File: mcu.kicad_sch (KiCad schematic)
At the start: 44 parts, among them J201 DISP, J202 SWD, J203 SPI, J204 USB serial, Q201 2N7002, SW201 Reset, U201 STM32F103CBT6, U202 USBLC6-2SC6, U203 AMS1117-3.3, Y201 8MHz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

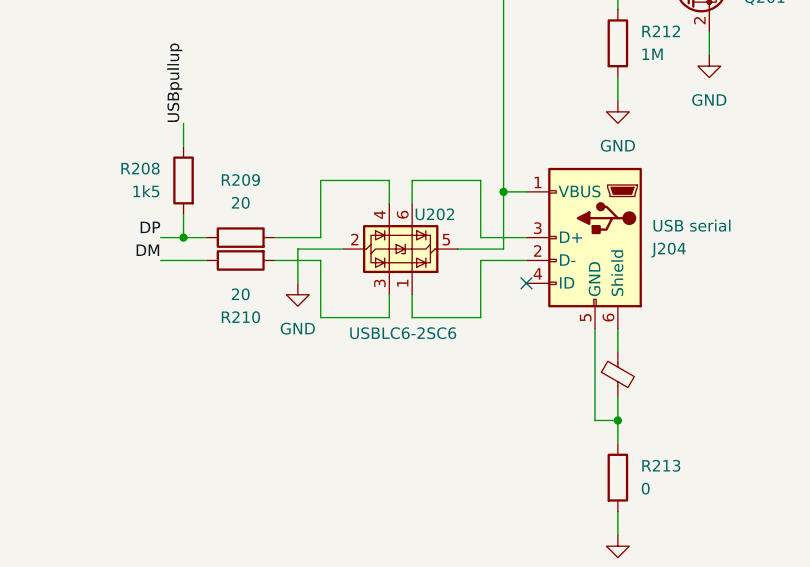
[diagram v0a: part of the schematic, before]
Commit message: Fix USB
Signed-off-by: Benedikt Spranger <b.spranger@linutronix.de>
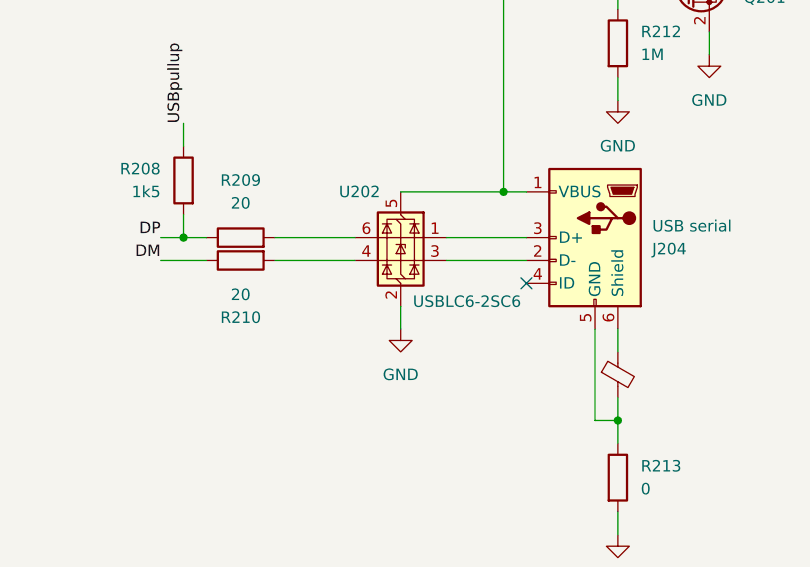
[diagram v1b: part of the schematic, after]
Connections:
- net at U202.1 (I/O1): now also J204.3 (D+); no longer J204.2 (D-)
- net at U202.3 (I/O2): now also J204.2 (D-); no longer R210.2
- net at U202.4 (I/O2): now also R210.2; no longer R209.2
- net at U202.6 (I/O1): now also R209.2; no longer J204.3 (D+)
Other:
- moved on the sheet: U202

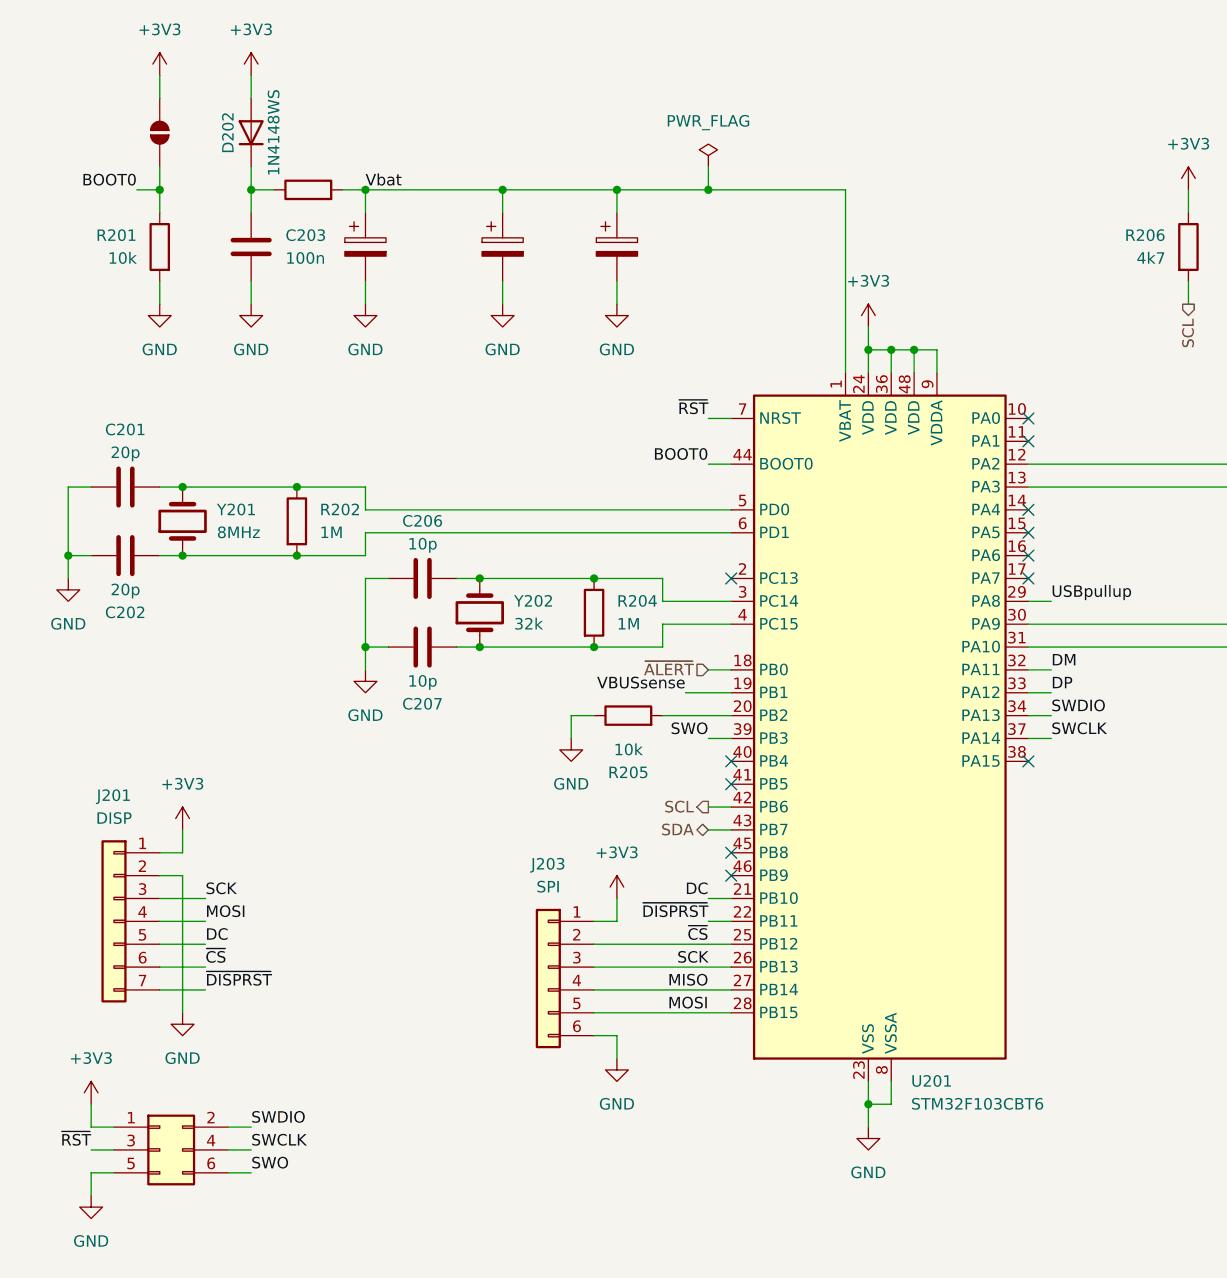
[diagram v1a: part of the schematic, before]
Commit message: Update to KiCAD 9.x
Signed-off-by: Benedikt Spranger <b.spranger@linutronix.de>
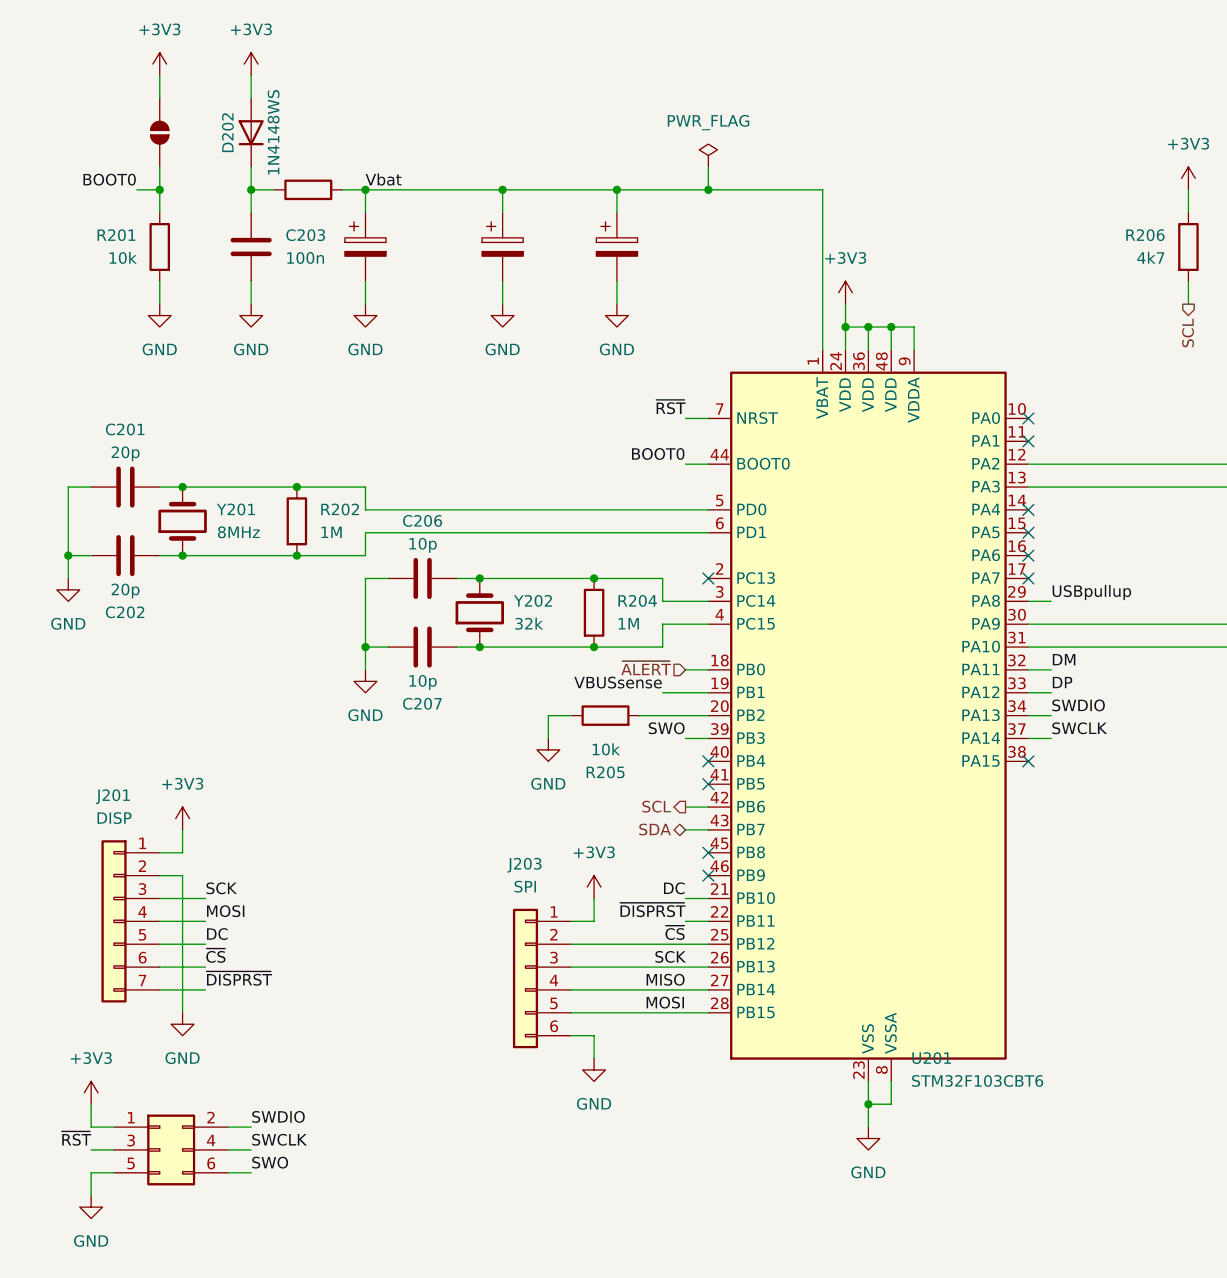
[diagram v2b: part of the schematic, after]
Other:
- moved on the sheet: J203, R205, U201

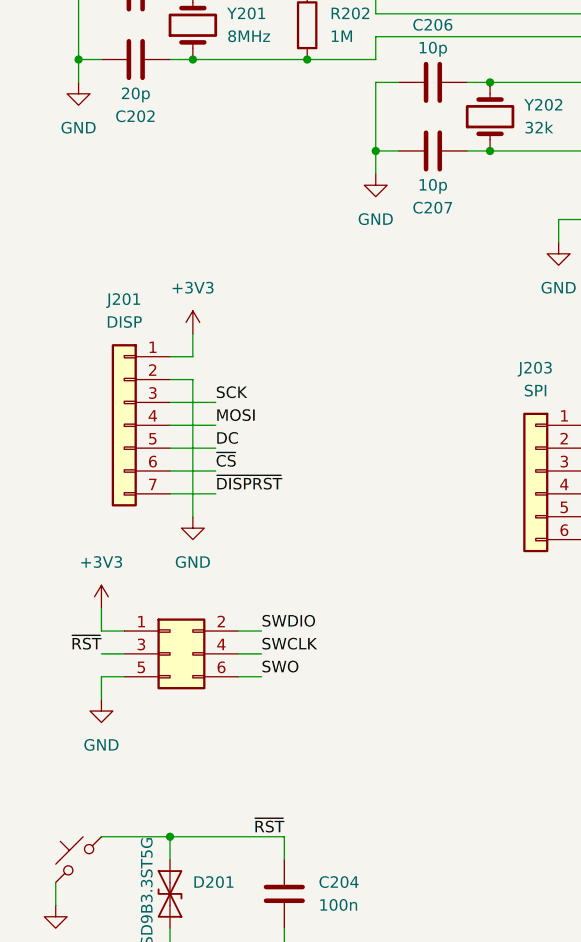
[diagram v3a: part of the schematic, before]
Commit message: Rework SWD connector
Signed-off-by: Benedikt Spranger <b.spranger@linutronix.de>
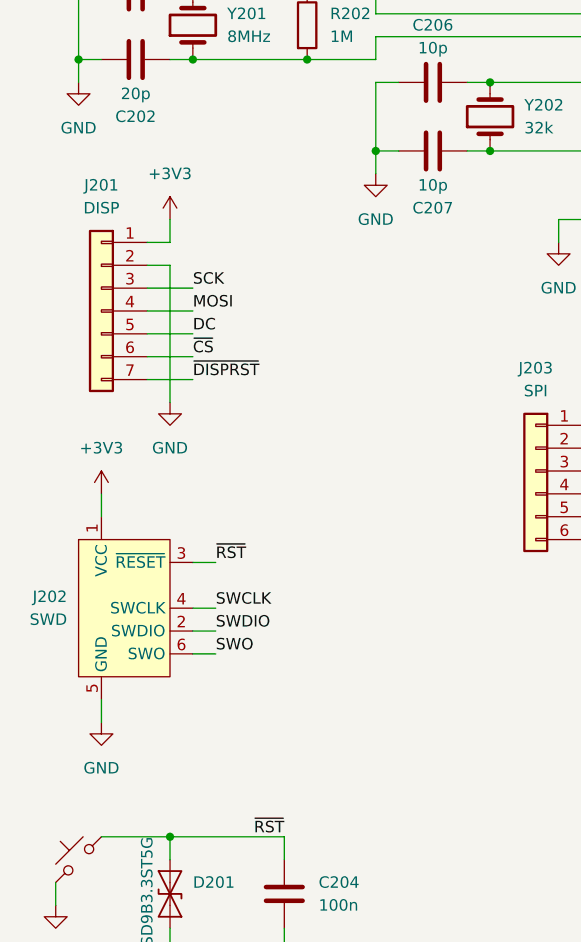
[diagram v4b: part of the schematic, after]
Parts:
- removed J202: SWD, Connector:Tag-Connect_TC2030-IDC-FP_2x03_P1.27mm_Vertical, symbol Connector_Generic:Conn_02x03_Odd_Even
- added J202: SWD, Connector:Tag-Connect_TC2030-IDC-FP_2x03_P1.27mm_Vertical, symbol Connector:Conn_ARM_SWD_TagConnect_TC2030
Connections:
- net +3V3: now also J202.1 (VCC)
- net GND: now also J202.5 (GND)
- net SWCLK: now also J202.4 (SWCLK)
- net SWDIO: now also J202.2 (SWDIO)
- net SWO: now also J202.6 (SWO)
- net ~{RST}: now also J202.3 (~{RESET})
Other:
- moved on the sheet: J201

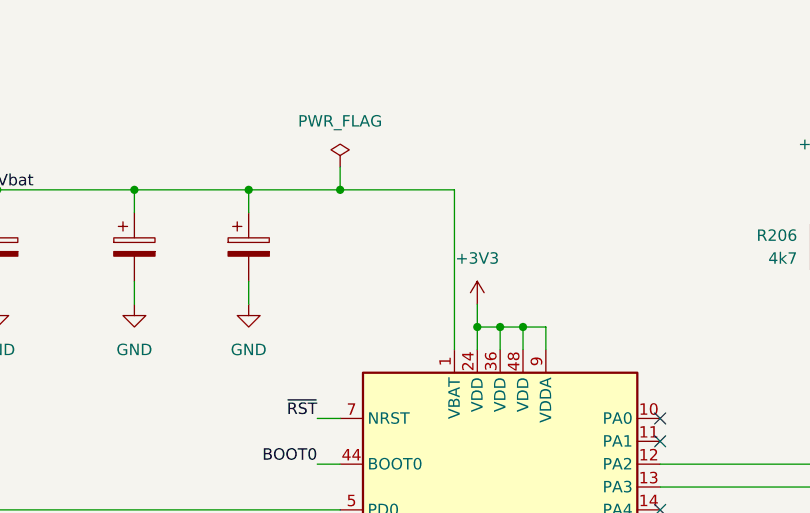
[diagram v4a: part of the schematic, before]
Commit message: Add BAT power disconnector
Signed-off-by: Benedikt Spranger <b.spranger@linutronix.de>
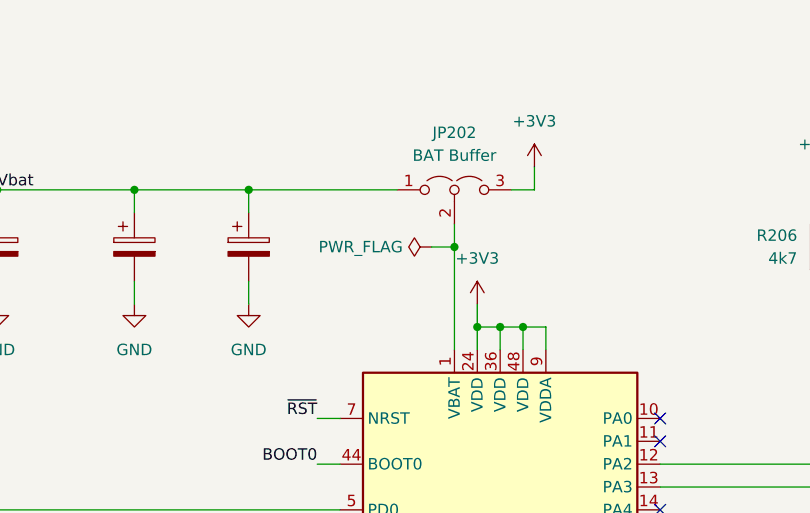
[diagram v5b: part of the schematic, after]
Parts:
- added JP202: BAT Buffer, Connector_PinHeader_2.54mm:PinHeader_1x03_P2.54mm_Vertical, symbol Jumper:Jumper_3_Open
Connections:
- net +3V3: now also JP202.3 (B)
- net Vbat: now also JP202.1 (A); no longer U201.1 (VBAT)
- new net: JP202.2 (C), U201.1 (VBAT)
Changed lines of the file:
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@@
 	)
 	(junction
-		(at 99.06 38.1)
-		(diameter 0)
-		(color 0 0 0 0)
-	)
-	(junction
 		(at 40.64 71.12)
 		(diameter 0)
@@
 	)
 	(junction
+		(at 111.76 44.45)
+		(diameter 0)
+		(color 0 0 0 0)
+	)
+	(junction
 		(at 116.84 139.7)
 		(diameter 0)
@@
 	(wire
 		(pts
+			(xy 111.76 41.91) (xy 111.76 44.45)
+		)
+		(stroke
+			(width 0)
+			(type default)
+		)
+	)
+	(wire
+		(pts
 			(xy 134.62 93.98) (xy 137.16 93.98)
 		)
@@
 	(wire
 		(pts
-			(xy 190.5 38.1) (xy 190.5 40.64)
+			(xy 111.76 44.45) (xy 111.76 55.88)
 		)
 		(stroke
@@
 	(wire
 		(pts
-			(xy 111.76 38.1) (xy 99.06 38.1)
+			(xy 190.5 38.1) (xy 190.5 40.64)
 		)
 		(stroke
@@
 	(wire
 		(pts
+			(xy 118.11 38.1) (xy 120.65 38.1)
+		)
+		(stroke
+			(width 0)
+			(type default)
+		)
+	)
+	(wire
+		(pts
 			(xy 152.4 38.1) (xy 152.4 40.64)
 		)
@@
 	(wire
 		(pts
+			(xy 109.22 44.45) (xy 111.76 44.45)
+		)
+		(stroke
+			(width 0)
+			(type default)
+		)
+	)
+	(wire
+		(pts
 			(xy 76.2 48.26) (xy 76.2 50.8)
 		)
@@
 	(wire
 		(pts
+			(xy 120.65 38.1) (xy 120.65 35.56)
+		)
+		(stroke
+			(width 0)
+			(type default)
+		)
+	)
+	(wire
+		(pts
 			(xy 96.52 68.58) (xy 99.06 68.58)
 		)
@@
 	(wire
 		(pts
-			(xy 88.9 38.1) (xy 99.06 38.1)
+			(xy 88.9 38.1) (xy 105.41 38.1)
 		)
 		(stroke
@@
 	(wire
 		(pts
-			(xy 99.06 35.56) (xy 99.06 38.1)
-		)
-		(stroke
-			(width 0)
-			(type default)
-		)
-	)
-	(wire
-		(pts
 			(xy 83.82 132.08) (xy 86.36 132.08)
 		)
@@
 	(wire
 		(pts
-			(xy 111.76 38.1) (xy 111.76 55.88)
-		)
-		(stroke
-			(width 0)
-			(type default)
-		)
-	)
-	(wire
-		(pts
 			(xy 119.38 53.34) (xy 119.38 55.88)
 		)
@@
 	)
 	(symbol
+		(lib_id "power:+3V3")
+		(at 120.65 35.56 0)
+		(unit 1)
+		(exclude_from_sim no)
+		(in_bom yes)
+		(on_board yes)
+		(dnp no)
+		(fields_autoplaced yes)
+		(property "Reference" "#PWR0242"
+			(at 120.65 39.37 0)
+			(effects
+				(font
+					(size 1.27 1.27)
+				)
+				(hide yes)
+			)
+		)
+		(property "Value" "+3V3"
+			(at 120.65 30.48 0)
+			(effects
+				(font
+					(size 1.27 1.27)
+				)
+			)
+		)
+		(property "Footprint" ""
+			(at 120.65 35.56 0)
+			(effects
+				(font
+					(size 1.27 1.27)
+				)
+				(hide yes)
+			)
+		)
+		(property "Datasheet" ""
+			(at 120.65 35.56 0)
+			(effects
+				(font
+					(size 1.27 1.27)
+				)
+				(hide yes)
+			)
+		)
+		(property "Description" "Power symbol creates a global label with name \"+3V3\""
+			(at 120.65 35.56 0)
+			(effects
+				(font
+					(size 1.27 1.27)
+				)
+				(hide yes)
+			)
+		)
+		(pin "1"
+		)
+		(instances
+			(project "akkupack-ng"
+				(path "/28c14643-513c-46b6-b18d-27cb3c7eee92/de76c23a-5b99-4def-922c-07fd05553b7c"
+					(reference "#PWR0242")
+					(unit 1)
+				)
+			)
+		)
+	)
+	(symbol
 		(lib_id "Device:FerriteBead_Small")
 		(at 254 134.62 0)
@@
 	(symbol
 		(lib_id "power:PWR_FLAG")
-		(at 99.06 35.56 0)
+		(at 109.22 44.45 90)
 		(unit 1)
 		(exclude_from_sim no)
@@
 		(on_board yes)
 		(dnp no)
-		(fields_autoplaced yes)
 		(property "Reference" "#FLG0201"
-			(at 99.06 33.655 0)
+			(at 107.315 44.45 0)
 			(effects
 				(font
@@
 		)
 		(property "Value" "PWR_FLAG"
-			(at 99.06 30.48 0)
+			(at 101.346 44.45 90)
 			(effects
 				(font
@@
 		)
 		(property "Footprint" ""
-			(at 99.06 35.56 0)
+			(at 109.22 44.45 0)
 			(effects
 				(font
@@
 		)
 		(property "Datasheet" "~"
-			(at 99.06 35.56 0)
+			(at 109.22 44.45 0)
 			(effects
 				(font
@@
 		)
 		(property "Description" "Special symbol for telling ERC where power comes from"
-			(at 99.06 35.56 0)
+			(at 109.22 44.45 0)
 			(effects
 				(font
@@
 					(unit 1)
 				)
+			)
+		)
+	)
+	(symbol
+		(lib_id "Jumper:Jumper_3_Open")
+		(at 111.76 38.1 0)
+		(unit 1)
+		(exclude_from_sim no)
+		(in_bom no)
+		(on_board yes)
+		(dnp no)
+		(fields_autoplaced yes)
+		(property "Reference" "JP202"
+			(at 111.76 31.75 0)
+			(effects
+				(font
+					(size 1.27 1.27)
+				)
+			)
+		)
+		(property "Value" "BAT Buffer"
+			(at 111.76 34.29 0)
+			(effects
+				(font
+					(size 1.27 1.27)
+				)
+			)
+		)
+		(property "Footprint" "Connector_PinHeader_2.54mm:PinHeader_1x03_P2.54mm_Vertical"
+			(at 111.76 38.1 0)
+			(effects
+				(font
+					(size 1.27 1.27)
+				)
+				(hide yes)
+			)
+		)
+		(property "Datasheet" "~"
+			(at 111.76 38.1 0)
+			(effects
+				(font
+					(size 1.27 1.27)
+				)
+				(hide yes)
+			)
+		)
+		(property "Description" "Jumper, 3-pole, both open"
+			(at 111.76 38.1 0)
+			(effects
+				(font
+					(size 1.27 1.27)
+				)
+				(hide yes)
+			)
+		)
+		(pin "2"
+		)
+		(pin "3"
+		)
+		(pin "1"
+		)
+		(instances
+			(project ""
+				(path "/28c14643-513c-46b6-b18d-27cb3c7eee92/de76c23a-5b99-4def-922c-07fd05553b7c"
+					(reference "JP202")
+					(unit 1)
+				)
